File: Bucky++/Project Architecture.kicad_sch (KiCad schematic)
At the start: 8 parts

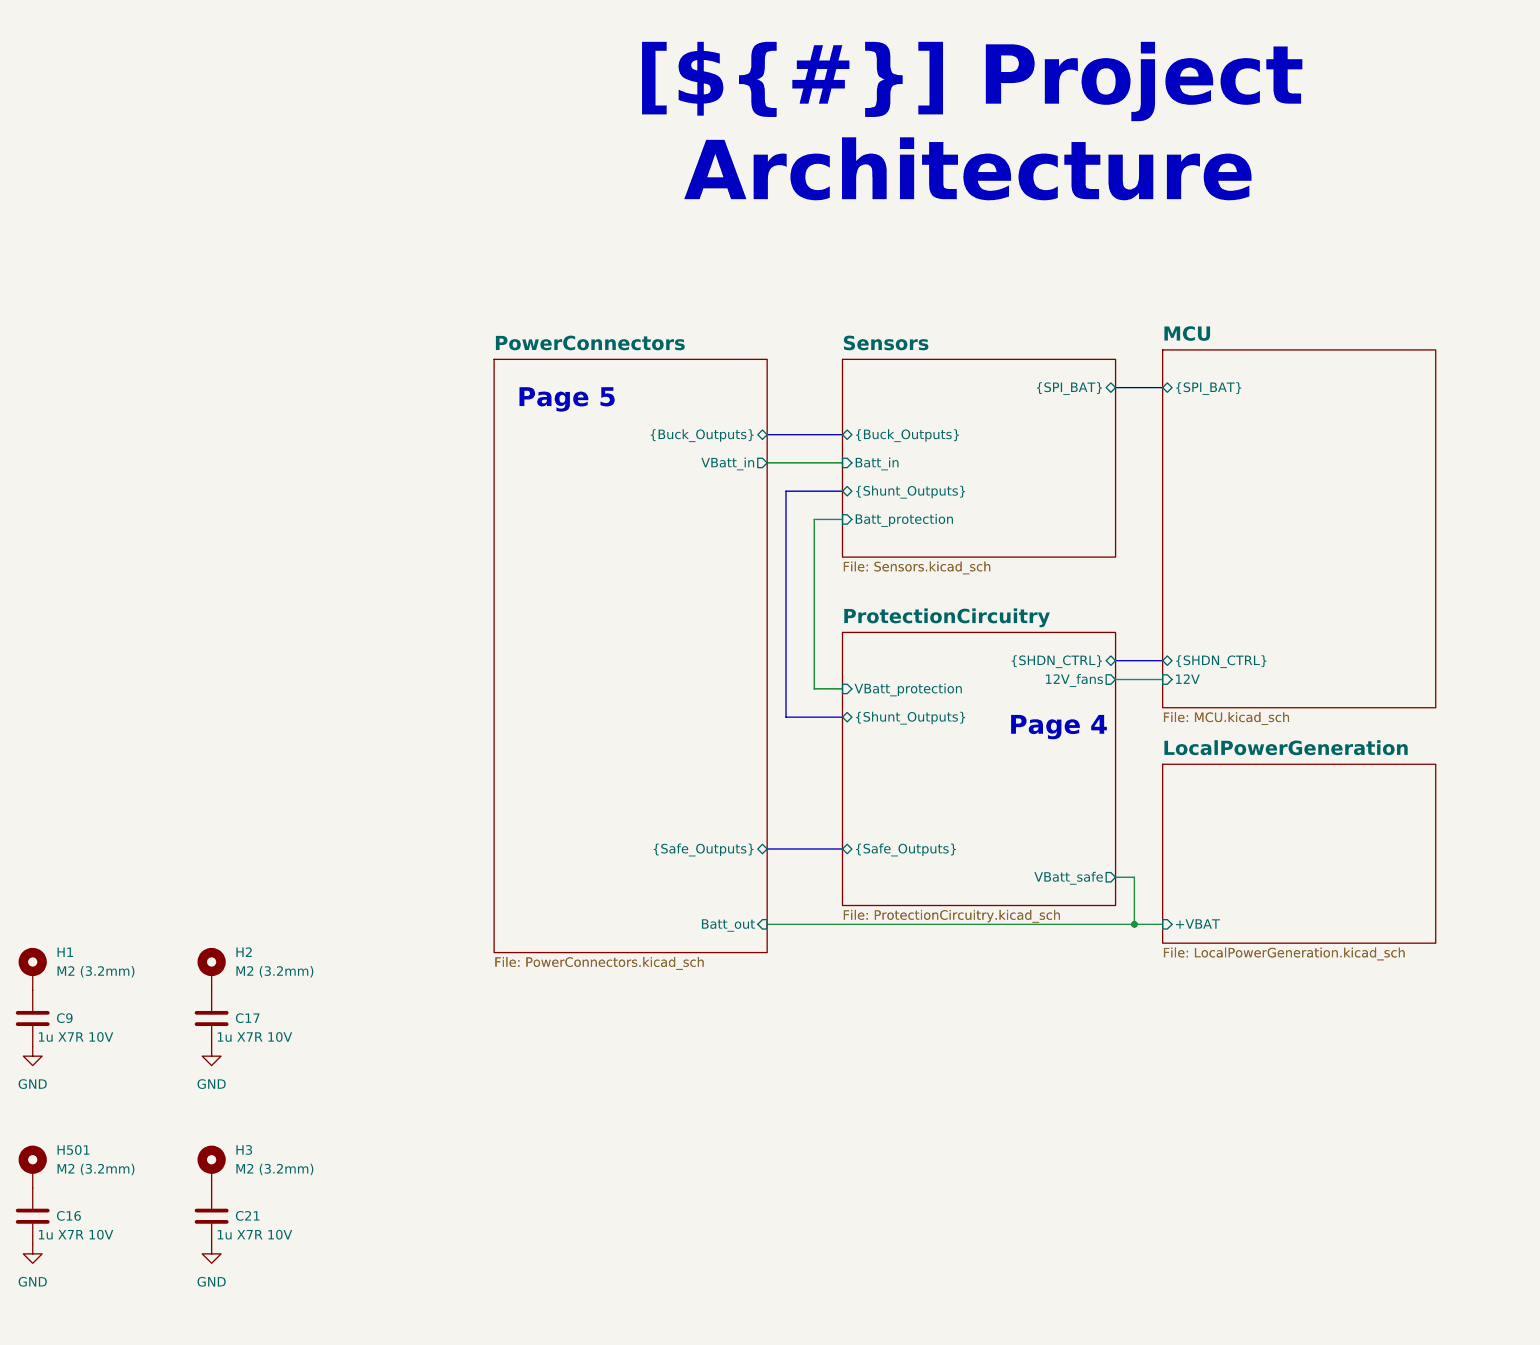
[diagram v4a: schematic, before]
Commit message: updated circuit after review. updated silkscreen
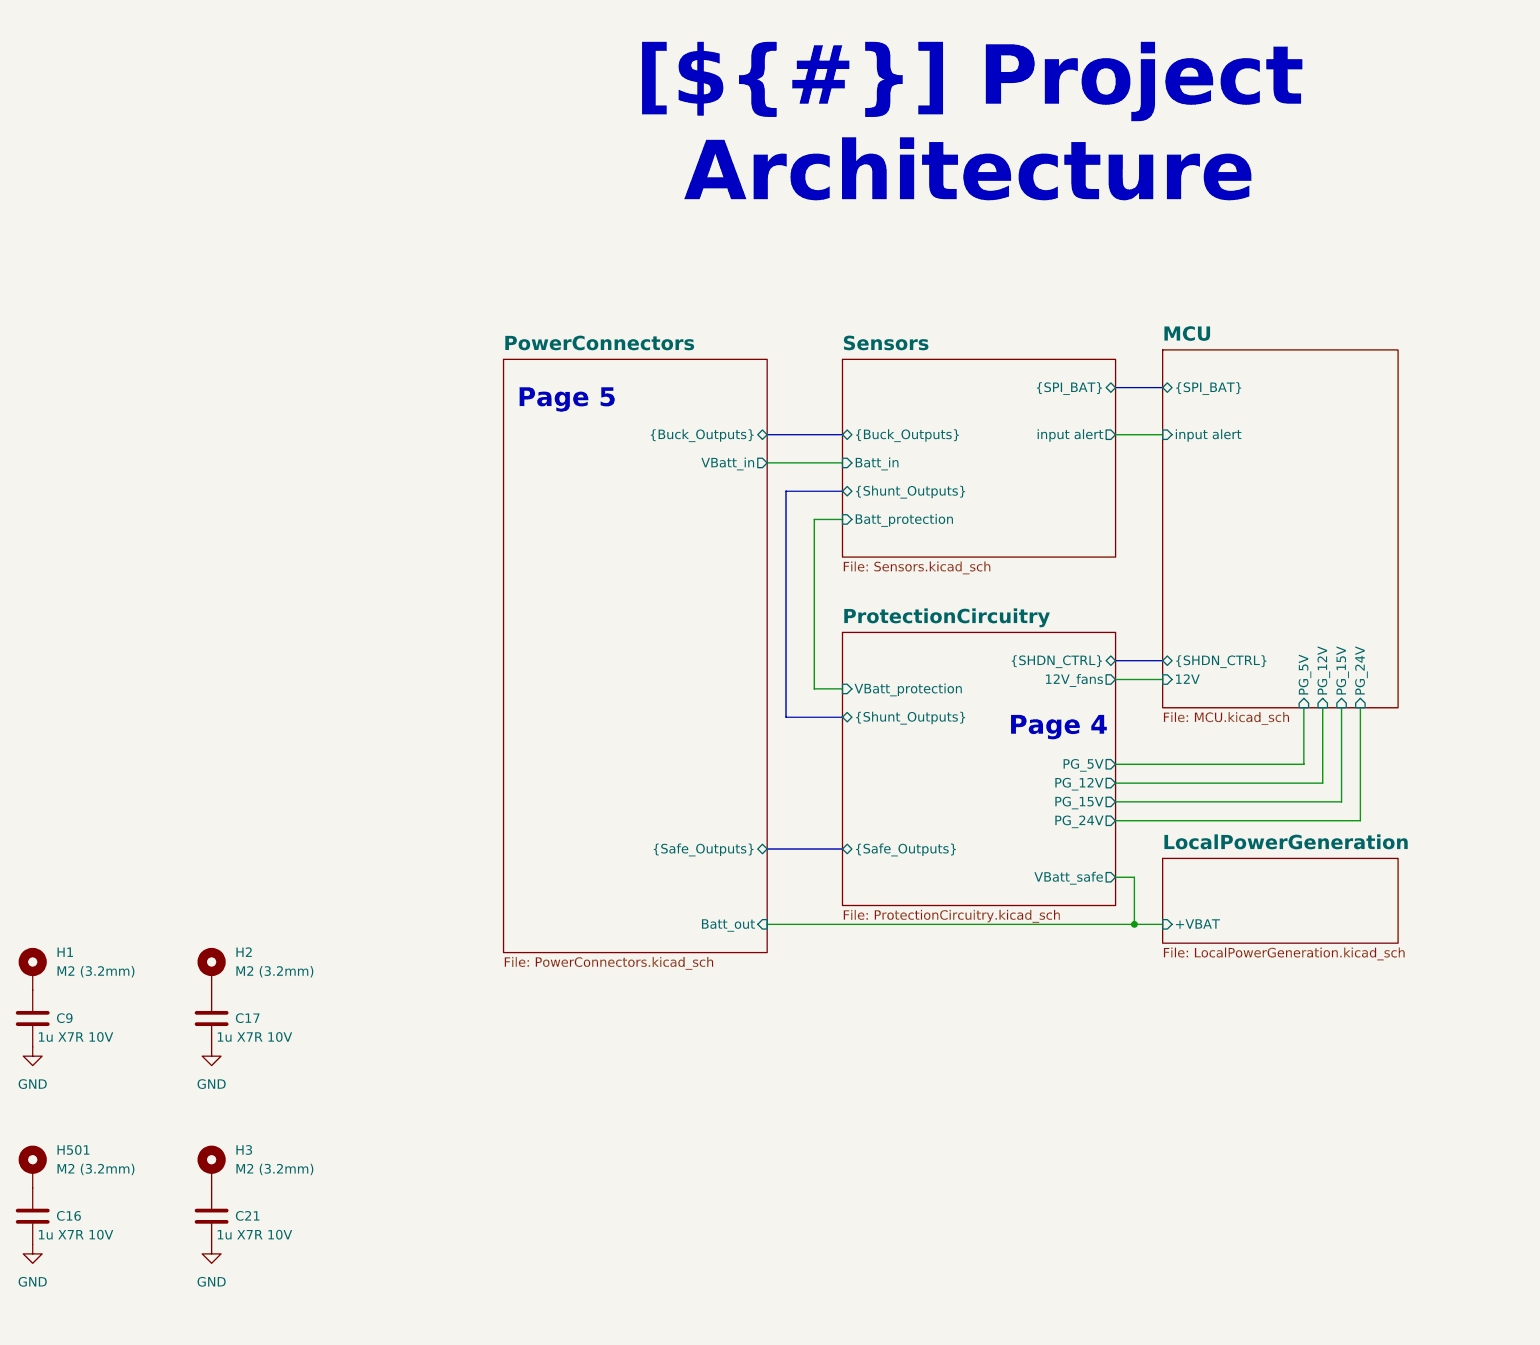
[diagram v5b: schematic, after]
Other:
- sheet MCU ports: added PG_12V, PG_15V, PG_24V, PG_5V, input alert; removed none
- sheet ProtectionCircuitry ports: added PG_12V, PG_15V, PG_24V, PG_5V; removed none
- sheet Sensors ports: added input alert; removed none
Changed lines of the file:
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@@
+		)
+	)
+	(wire
+		(pts
+			(xy 165.1 118.11) (xy 193.04 118.11)
+		)
+		(stroke
+			(width 0)
+			(type default)
 		)
 	)
@@
 	(wire
 		(pts
+			(xy 165.1 115.57) (xy 190.5 115.57)
+		)
+		(stroke
+			(width 0)
+			(type default)
+		)
+	)
+	(wire
+		(pts
+			(xy 165.1 123.19) (xy 198.12 123.19)
+		)
+		(stroke
+			(width 0)
+			(type default)
+		)
+	)
+	(wire
+		(pts
 			(xy 165.1 104.14) (xy 171.45 104.14)
 		)
@@
 	(wire
 		(pts
+			(xy 198.12 123.19) (xy 198.12 107.95)
+		)
+		(stroke
+			(width 0)
+			(type default)
+		)
+	)
+	(wire
+		(pts
+			(xy 165.1 120.65) (xy 195.58 120.65)
+		)
+		(stroke
+			(width 0)
+			(type default)
+		)
+	)
+	(wire
+		(pts
 			(xy 124.46 82.55) (xy 124.46 105.41)
 		)
@@
 	(wire
 		(pts
+			(xy 165.1 71.12) (xy 171.45 71.12)
+		)
+		(stroke
+			(width 0)
+			(type default)
+		)
+	)
+	(wire
+		(pts
 			(xy 118.11 137.16) (xy 167.64 137.16)
 		)
@@
 		)
 	)
+	(wire
+		(pts
+			(xy 193.04 118.11) (xy 193.04 107.95)
+		)
+		(stroke
+			(width 0)
+			(type default)
+		)
+	)
 	(bus
 		(pts
 			(xy 165.1 101.6) (xy 171.45 101.6)
+		)
+		(stroke
+			(width 0)
+			(type default)
+		)
+	)
+	(wire
+		(pts
+			(xy 195.58 120.65) (xy 195.58 107.95)
+		)
+		(stroke
+			(width 0)
+			(type default)
+		)
+	)
+	(wire
+		(pts
+			(xy 190.5 115.57) (xy 190.5 107.95)
 		)
 		(stroke
@@
 			)
 		)
+		(pin "input alert" output
+			(at 165.1 71.12 0)
+			(effects
+				(font
+					(size 1.27 1.27)
+				)
+				(justify right)
+			)
+		)
 		(instances
 			(project "Bucky++"
@@
 	)
 	(sheet
-		(at 81.28 60.96)
-		(size 36.83 80.01)
+		(at 82.55 60.96)
+		(size 35.56 80.01)
 		(exclude_from_sim no)
 		(in_bom yes)
@@
 		)
 		(property "Sheetname" "PowerConnectors"
-			(at 81.28 59.9309 0)
+			(at 82.55 59.9309 0)
 			(effects
 				(font
@@
 		)
 		(property "Sheetfile" "PowerConnectors.kicad_sch"
-			(at 81.28 141.5546 0)
+			(at 82.55 141.5546 0)
 			(effects
 				(font
@@
 	)
 	(sheet
-		(at 171.45 115.57)
-		(size 36.83 24.13)
+		(at 171.45 128.27)
+		(size 31.75 11.43)
 		(exclude_from_sim no)
 		(in_bom yes)
@@
 		)
 		(property "Sheetname" "LocalPowerGeneration"
-			(at 171.45 114.5409 0)
+			(at 171.45 127.2409 0)
 			(effects
 				(font
@@
 	(sheet
 		(at 171.45 59.69)
-		(size 36.83 48.26)
+		(size 31.75 48.26)
 		(exclude_from_sim no)
 		(in_bom yes)
@@
 		(pin "12V" input
 			(at 171.45 104.14 180)
+			(effects
+				(font
+					(size 1.27 1.27)
+				)
+				(justify left)
+			)
+		)
+		(pin "input alert" input
+			(at 171.45 71.12 180)
+			(effects
+				(font
+					(size 1.27 1.27)
+				)
+				(justify left)
+			)
+		)
+		(pin "PG_5V" input
+			(at 190.5 107.95 270)
+			(effects
+				(font
+					(size 1.27 1.27)
+				)
+				(justify left)
+			)
+		)
+		(pin "PG_12V" input
+			(at 193.04 107.95 270)
+			(effects
+				(font
+					(size 1.27 1.27)
+				)
+				(justify left)
+			)
+		)
+		(pin "PG_15V" input
+			(at 195.58 107.95 270)
+			(effects
+				(font
+					(size 1.27 1.27)
+				)
+				(justify left)
+			)
+		)
+		(pin "PG_24V" input
+			(at 198.12 107.95 270)
 			(effects
 				(font
@@
 			(effects
 				(font
+					(size 1.27 1.27)
+				)
+				(justify right)
+			)
+		)
+		(pin "PG_24V" output
+			(at 165.1 123.19 0)
+			(effects
+				(font
+					(size 1.27 1.27)
+				)
+				(justify right)
+			)
+		)
+		(pin "PG_12V" output
+			(at 165.1 118.11 0)
+			(effects
+				(font
+					(size 1.27 1.27)
+				)
+				(justify right)
+			)
+		)
+		(pin "PG_5V" output
+			(at 165.1 115.57 0)
+			(effects
+				(font
+					(size 1.27 1.27)
+				)
+				(justify right)
+			)
+		)
+		(pin "PG_15V" output
+			(at 165.1 120.65 0)
+			(effects
+				(font

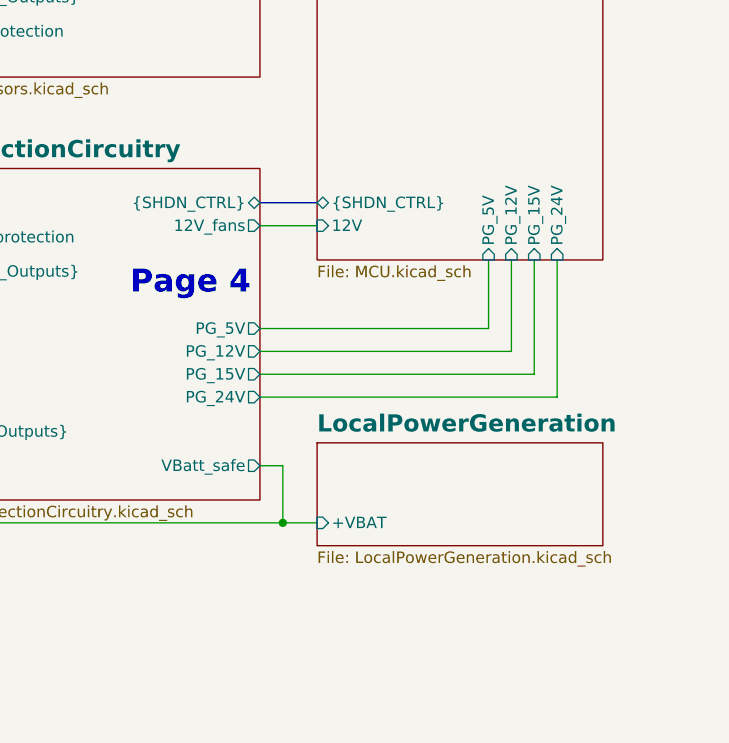
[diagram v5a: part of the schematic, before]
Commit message: fix layout and tolerance issues, started working on routing alerts
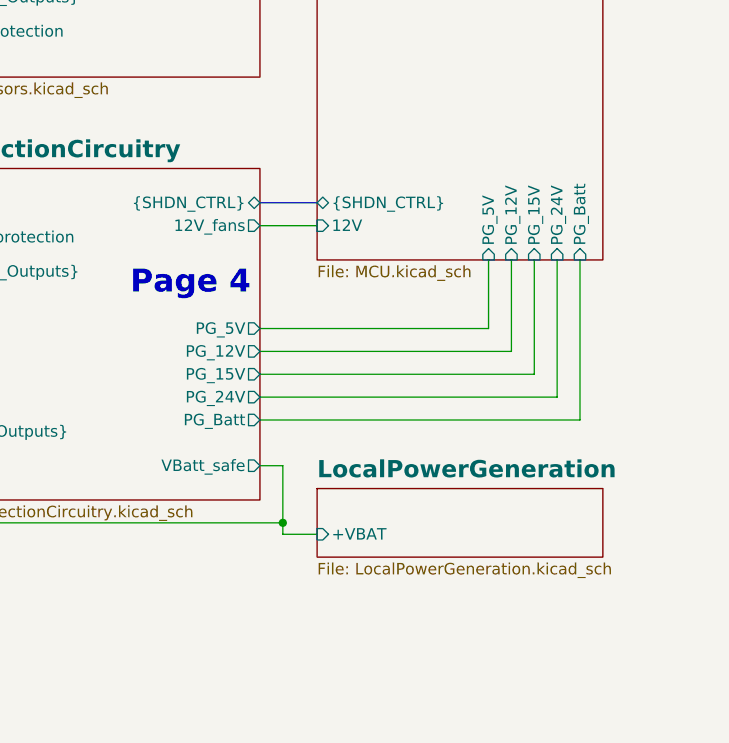
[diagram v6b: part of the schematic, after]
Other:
- sheet MCU ports: added PG_Batt; removed none
- sheet ProtectionCircuitry ports: added PG_Batt; removed none
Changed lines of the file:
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@@
 		(color 0 0 0 0)
 	)
+	(wire
+		(pts
+			(xy 200.66 125.73) (xy 200.66 107.95)
+		)
+		(stroke
+			(width 0)
+			(type default)
+		)
+	)
+	(wire
+		(pts
+			(xy 165.1 125.73) (xy 200.66 125.73)
+		)
+		(stroke
+			(width 0)
+			(type default)
+		)
+	)
 	(bus
 		(pts
@@
 	(wire
 		(pts
-			(xy 167.64 137.16) (xy 171.45 137.16)
+			(xy 167.64 138.43) (xy 171.45 138.43)
 		)
 		(stroke
@@
 		(pts
 			(xy 128.27 78.74) (xy 120.65 78.74)
+		)
+		(stroke
+			(width 0)
+			(type default)
+		)
+	)
+	(wire
+		(pts
+			(xy 167.64 138.43) (xy 167.64 137.16)
 		)
 		(stroke
@@
 	)
 	(sheet
-		(at 171.45 128.27)
-		(size 31.75 11.43)
+		(at 171.45 133.35)
+		(size 31.75 7.62)
 		(exclude_from_sim no)
 		(in_bom yes)
@@
 		)
 		(property "Sheetname" "LocalPowerGeneration"
-			(at 171.45 127.2409 0)
+			(at 171.45 132.3209 0)
 			(effects
 				(font
@@
 		)
 		(property "Sheetfile" "LocalPowerGeneration.kicad_sch"
-			(at 171.45 140.2846 0)
+			(at 171.45 141.5546 0)
 			(effects
 				(font
@@
 		)
 		(pin "+VBAT" input
-			(at 171.45 137.16 180)
+			(at 171.45 138.43 180)
 			(effects
 				(font
@@
 			)
 		)
+		(pin "PG_Batt" input
+			(at 200.66 107.95 270)
+			(effects
+				(font
+					(size 1.27 1.27)
+				)
+				(justify left)
+			)
+		)
 		(instances
 			(project "Bucky++"
@@
 			(effects
 				(font
+					(size 1.27 1.27)
+				)
+				(justify right)
+			)
+		)
+		(pin "PG_Batt" output
+			(at 165.1 125.73 0)
+			(effects
+				(font

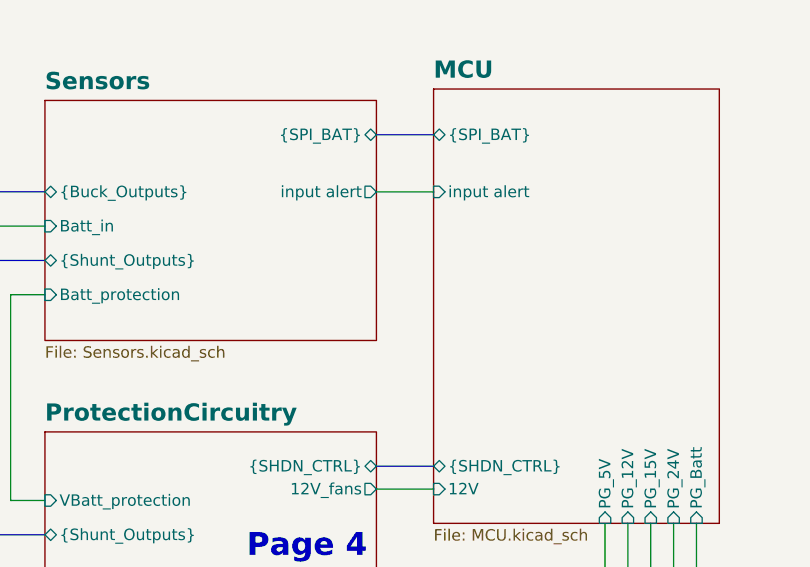
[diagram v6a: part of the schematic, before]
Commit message: connected alert pins of each rail
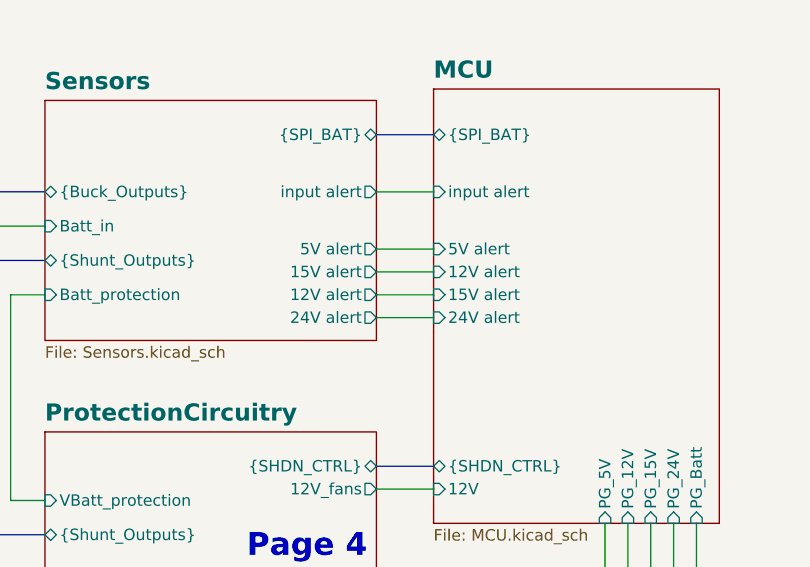
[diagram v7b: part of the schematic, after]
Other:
- sheet MCU ports: added 12V alert, 15V alert, 24V alert, 5V alert; removed none
- sheet Sensors ports: added 12V alert, 15V alert, 24V alert, 5V alert; removed none
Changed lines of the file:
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@@
+	(wire
+		(pts
+			(xy 165.1 77.47) (xy 171.45 77.47)
+		)
+		(stroke
+			(width 0)
+			(type default)
+		)
+	)
 	(wire
 		(pts
@@
 	(wire
 		(pts
+			(xy 165.1 80.01) (xy 171.45 80.01)
+		)
+		(stroke
+			(width 0)
+			(type default)
+		)
+	)
+	(wire
+		(pts
 			(xy 124.46 82.55) (xy 124.46 105.41)
 		)
@@
 		(pts
 			(xy 195.58 120.65) (xy 195.58 107.95)
+		)
+		(stroke
+			(width 0)
+			(type default)
+		)
+	)
+	(wire
+		(pts
+			(xy 165.1 82.55) (xy 171.45 82.55)
+		)
+		(stroke
+			(width 0)
+			(type default)
+		)
+	)
+	(wire
+		(pts
+			(xy 165.1 85.09) (xy 171.45 85.09)
 		)
 		(stroke
@@
 			)
 		)
+		(pin "24V alert" output
+			(at 165.1 85.09 0)
+			(effects
+				(font
+					(size 1.27 1.27)
+				)
+				(justify right)
+			)
+		)
+		(pin "5V alert" output
+			(at 165.1 77.47 0)
+			(effects
+				(font
+					(size 1.27 1.27)
+				)
+				(justify right)
+			)
+		)
+		(pin "15V alert" output
+			(at 165.1 80.01 0)
+			(effects
+				(font
+					(size 1.27 1.27)
+				)
+				(justify right)
+			)
+		)
+		(pin "12V alert" output
+			(at 165.1 82.55 0)
+			(effects
+				(font
+					(size 1.27 1.27)
+				)
+				(justify right)
+			)
+		)
 		(instances
 			(project "Bucky++"
@@
 			(effects
 				(font
+					(size 1.27 1.27)
+				)
+				(justify left)
+			)
+		)
+		(pin "24V alert" input
+			(at 171.45 85.09 180)
+			(effects
+				(font
+					(size 1.27 1.27)
+				)
+				(justify left)
+			)
+		)
+		(pin "15V alert" input
+			(at 171.45 82.55 180)
+			(effects
+				(font
+					(size 1.27 1.27)
+				)
+				(justify left)
+			)
+		)
+		(pin "12V alert" input
+			(at 171.45 80.01 180)
+			(effects
+				(font
+					(size 1.27 1.27)
+				)
+				(justify left)
+			)
+		)
+		(pin "5V alert" input
+			(at 171.45 77.47 180)
+			(effects
+				(font

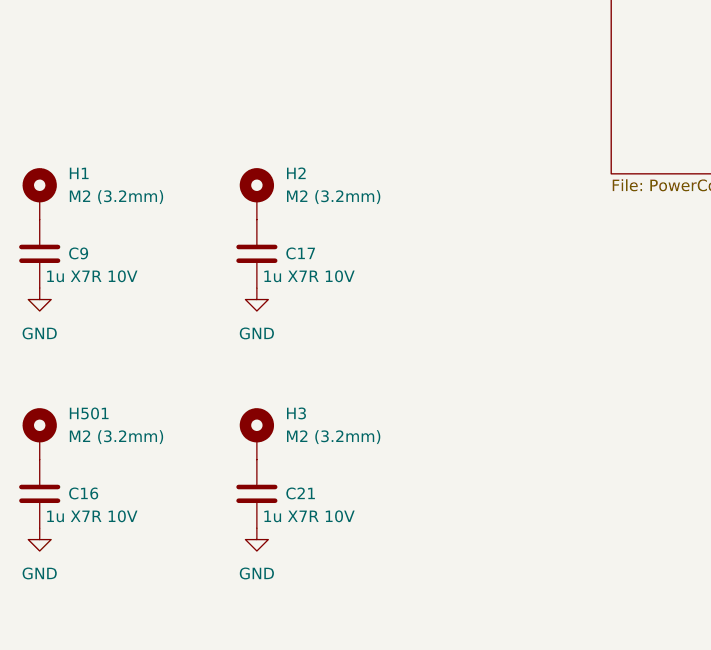
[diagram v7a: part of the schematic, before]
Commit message: Cleared DRC errors, corrected routing errors, cleaned the schematic
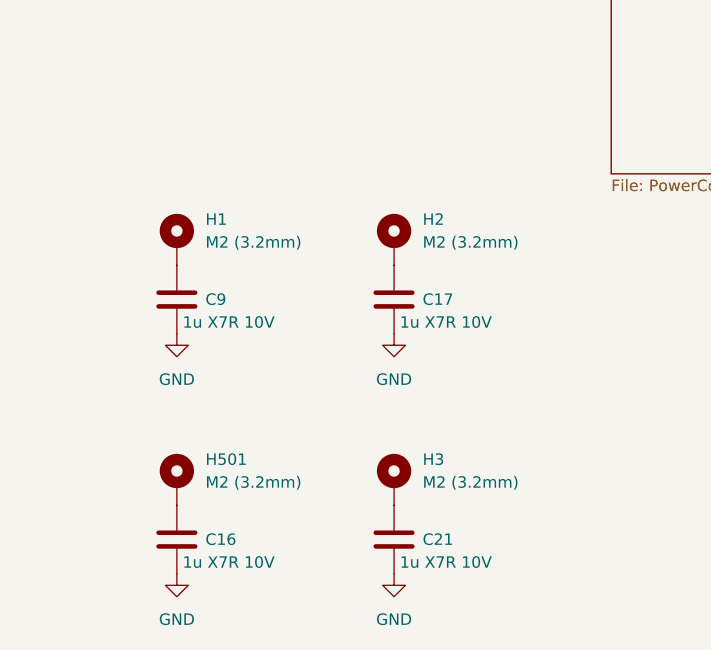
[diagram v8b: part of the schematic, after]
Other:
- moved on the sheet: C16, C17, C21, C9, H1, H2, H3, H501
